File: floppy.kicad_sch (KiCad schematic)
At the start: 42 parts, among them J7 DB23_Female_MountingHoles, J8 Conn_02x13_Odd_Even, J9 Conn_01x04, U8 MT3608, U9 SN74LS06NSR

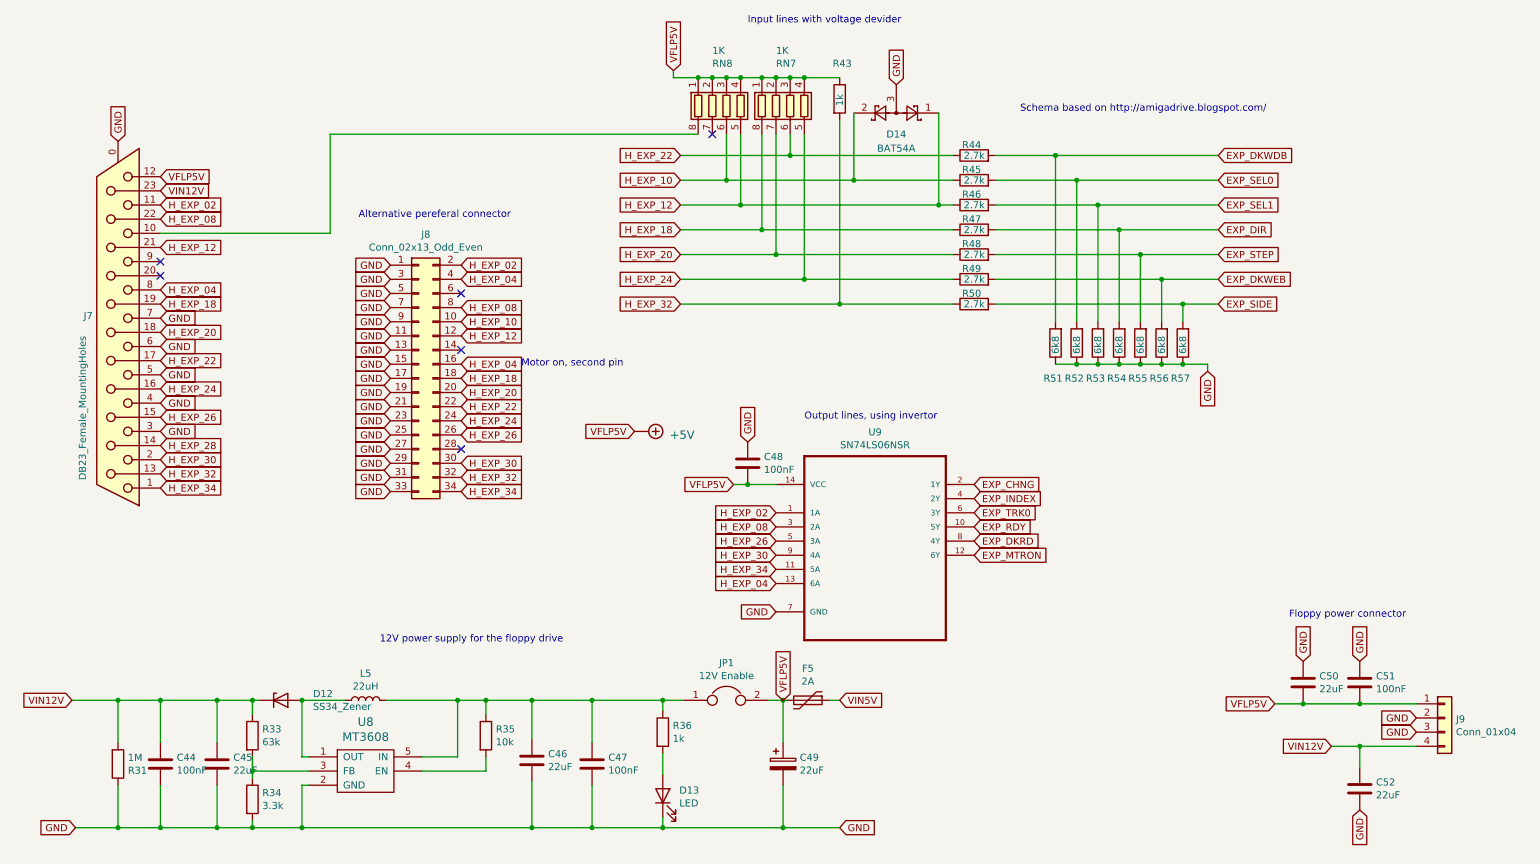
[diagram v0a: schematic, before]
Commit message: Fixed board for Kicad 6, replaced some missing footprints.
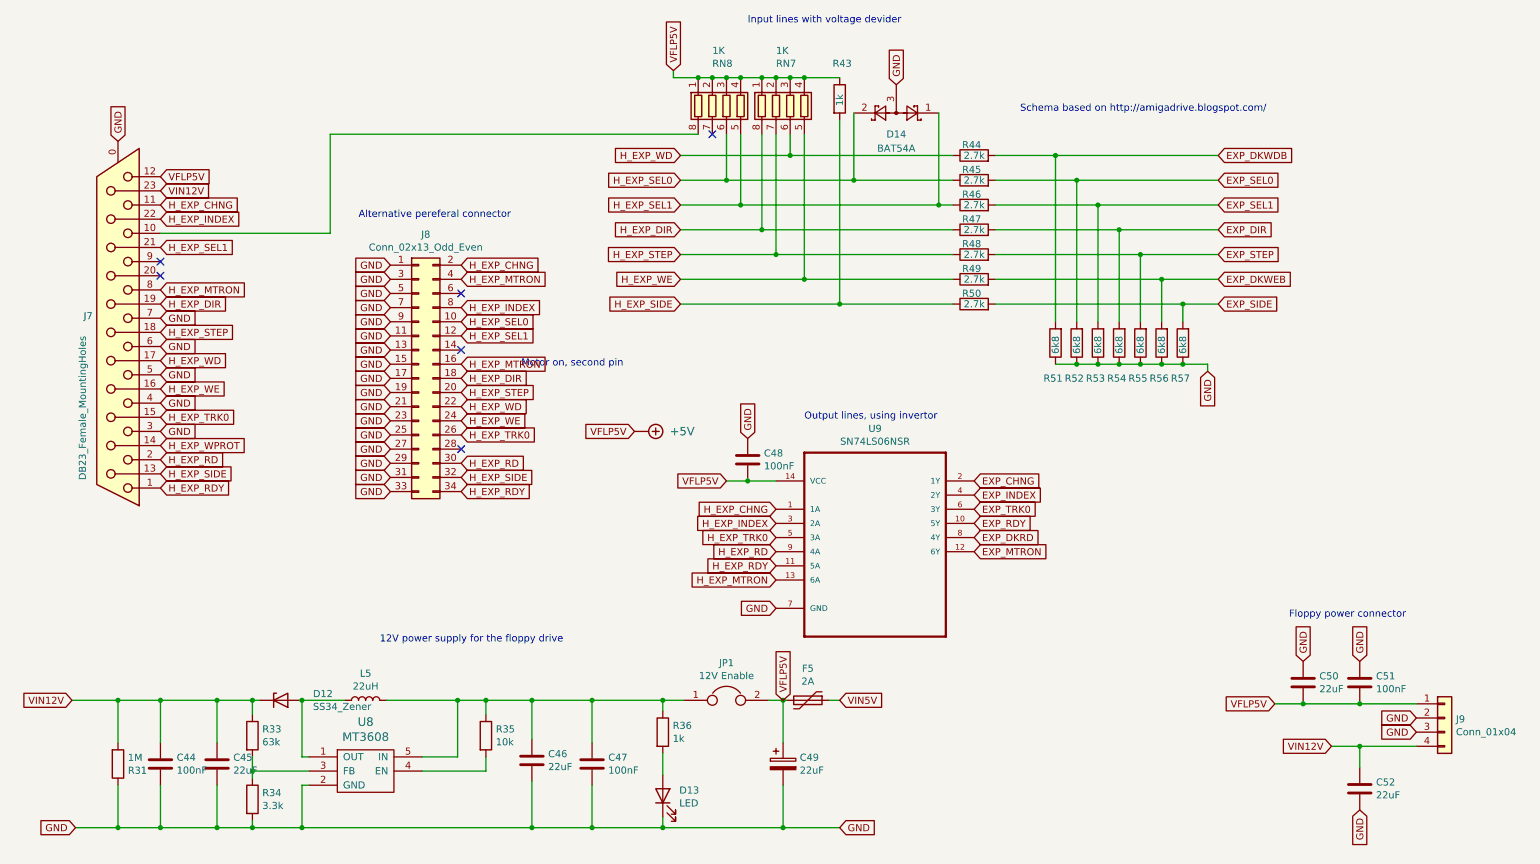
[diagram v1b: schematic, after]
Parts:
- U9: footprint SOIC127P780X200-14N -> Package_SO:SO-14_5.3x10.2mm_P1.27mm
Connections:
- net H_EXP_02 renamed H_EXP_CHNG
- net H_EXP_04 renamed H_EXP_MTRON
- net H_EXP_08 renamed H_EXP_INDEX
- net H_EXP_10 renamed H_EXP_SEL0
- net H_EXP_12 renamed H_EXP_SEL1
- net H_EXP_18 renamed H_EXP_DIR
- net H_EXP_20 renamed H_EXP_STEP
- net H_EXP_22 renamed H_EXP_WD
- net H_EXP_24 renamed H_EXP_WE
- net H_EXP_26 renamed H_EXP_TRK0
- net H_EXP_28 renamed H_EXP_WPROT
- net H_EXP_30 renamed H_EXP_RD
- net H_EXP_32 renamed H_EXP_SIDE
- net H_EXP_34 renamed H_EXP_RDY
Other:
- moved on the sheet: C48
